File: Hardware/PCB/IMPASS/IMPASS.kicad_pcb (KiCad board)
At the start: 2 copper layers, 73.9 x 100 mm, 192 parts, among them J1 POWER, J11 SOLENOIDES, J17 PUENTE H_1, J18 PUENTE H_2, J19 SOLENOIDES, J2 POWER, J20 SENSORES, J21 PROG, J22 VM, J23 EJE1, J24 EJE2, J25 EJE3, J26 SOLENOIDES, J27 PUENTE H, J28 PUENTE H, J29 SENSORES, Q1 BC847BDW1, Q10 BC847BDW1, Q11 DMN3008SFG, Q12 DMN3008SFG, Q13 DMP3013SFV, Q14 DMP3013SFV, Q15 DMN3008SFG, Q16 DMN3008SFG, Q17 BC847BDW1, Q18 DMP3013SFV, Q19 DMN3008SFG, Q2 DMP3013SFV, Q20 DMN3008SFG, Q21 DMP3013SFV, Q22 BC847BDW1, Q23 DMN3008SFG, Q24 DMN3008SFG, Q25 DMP3013SFV, Q26 DMP3013SFV, Q3 DMP3013SFV, Q4 DMP3013SFV, Q43 DMN3008SFG, Q44 DMN3008SFG, Q45 DMN3008SFG, Q49 2N7002, Q5 BC847BDW1, Q50 2N7002, Q51 2N7002, Q52 2N7002, Q53 2N7002, Q54 2N7002, Q55 2N7002, Q56 2N7002, Q57 2N7002, Q58 2N7002, Q59 2N7002, Q6 DMP3013SFV, Q60 2N7002, Q61 2N7002, Q62 2N7002, Q63 2N7002, Q64 2N7002, Q65 2N7002, Q66 2N7002, Q67 2N7002, Q68 2N7002, Q69 2N7002, Q7 BC847BDW1, Q71 DMN3008SFG, Q73 DMN3008SFG, Q75 DMN3008SFG, Q77 DMN3008SFG, Q8 DMP3013SFV, Q9 DMP3013SFV, SW1 RESET, SW2 BOOT, U1 TPS62162DSG, U10 LIS3DH, U13 MCP3008, U14 ESP32-S3-WROOM-1, U15 TPS62163DSG, U2 LM75B, U3 ACS712xLCTR-30A, U4 ACS712xLCTR-30A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

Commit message: Hardware: Update all the logic pcb 	- added ads1015 	- added the logic foe P-MOSFET 	- added I2C connector
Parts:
- removed D1, D2, D3, D4, D5, D6: 1N4448, Diode_THT:D_DO-35_SOD27_P2.54mm_Vertical_AnodeUp
- removed D8, D9: LED, LED_SMD:LED_0603_1608Metric
- removed R21, R22, R23, R24, R25, R26: 2k, Resistor_SMD:R_0603_1608Metric
- removed R34, R85: 100, Resistor_SMD:R_0603_1608Metric
- added C29: 100nF, Capacitor_SMD:C_0603_1608Metric, F.Cu at (146.2, 101.3)
- added C30: 100nF, Capacitor_SMD:C_0603_1608Metric, F.Cu at (120.1, 123.6)
- added C31: 100nF, Capacitor_SMD:C_0603_1608Metric, F.Cu at (112.6, 123.7)
- added J30: I2C, Connector_PinHeader_2.54mm:PinHeader_1x04_P2.54mm_Horizontal, F.Cu at (122.1, 128.7)
- added R89: 10k, Resistor_SMD:R_0603_1608Metric, F.Cu at (136.2, 101.4)
- added R90: 10k, Resistor_SMD:R_0603_1608Metric, F.Cu at (137.8, 100.6)
- added R91: 36k, Resistor_SMD:R_0603_1608Metric, F.Cu at (142.2, 98.2)
- added R92: 100k, Resistor_SMD:R_0603_1608Metric, F.Cu at (138.9, 98.2)
- added R93: 47k, Resistor_SMD:R_0603_1608Metric, F.Cu at (147.8, 99.4)
- added R94: 68k, Resistor_SMD:R_0603_1608Metric, F.Cu at (145.4, 98.2)
- added R95: 10k, Resistor_SMD:R_0603_1608Metric, F.Cu at (113.9, 121.1)
- added R96: 10k, Resistor_SMD:R_0603_1608Metric, F.Cu at (118.2, 121.1)
- added R97: 10k, Resistor_SMD:R_0603_1608Metric, F.Cu at (113.7, 126.1)
- added R98: 10k, Resistor_SMD:R_0603_1608Metric, F.Cu at (117.5, 126.1)
- added R99: 10k, Resistor_SMD:R_0603_1608Metric, F.Cu at (110.9, 121.5)
- added U11: TCA9406DC, Package_SO:SSOP-8_2.95x2.8mm_P0.65mm, F.Cu at (116.3, 123.6)
- added U12: ADS1015IDGS, Package_SO:TSSOP-10_3x3mm_P0.5mm, F.Cu at (141.9, 101.2)
- moved U8 107.1 mm to (54.3, 65.0), turned to 0 degrees
- moved C23 98.0 mm to (64.5, 33.4)
- moved U7 94.7 mm to (54.3, 58.4), turned to 0 degrees
- moved C25 93.2 mm to (68.5, 25.9), turned to 0 degrees
- moved C22 88.3 mm to (64.5, 30.9)
- moved Q18 85.4 mm to (75.3, 24.6), turned to 0 degrees
- moved U6 82.5 mm to (54.3, 51.8), turned to 0 degrees
- moved Q23 81.3 mm to (86.2, 24.6), turned to 0 degrees
- moved C26 81.2 mm to (68.5, 28.4), turned to 0 degrees
- moved Q24 80.9 mm to (86.2, 29.5), turned to 0 degrees
- moved Q25 80.6 mm to (91.6, 24.6), turned to 0 degrees
- moved Q21 80.2 mm to (80.8, 29.5), turned to 0 degrees
- moved Q26 80.1 mm to (91.6, 29.5), turned to 0 degrees
- moved Q20 79.1 mm to (80.8, 24.6), turned to 0 degrees
- moved Q19 78.7 mm to (75.3, 29.5), turned to 0 degrees
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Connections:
- C4 pad 1: /12v -> +12V
- J1 pad 1: /12v -> +12V
- Q1 pad 1: GND1 -> GND
- Q1 pad 3: Net-(Q1B-C2) -> /Placa_logica/logica_puente_h/PWM1
- Q1 pad 4: GND1 -> GND
- Q1 pad 6: Net-(Q1A-C1) -> /Placa_logica/logica_puente_h/~PWM1
- Q10 pad 1: GND1 -> GND
- Q10 pad 3: Net-(Q10B-C2) -> /Placa_logica/logica_puente_h/PWM4
- Q10 pad 4: GND1 -> GND
- Q10 pad 6: Net-(Q10A-C1) -> /Placa_logica/logica_puente_h/~PWM4
- Q13 pad 4: Net-(Q10A-C1) -> /Placa_potencia/Eje2/PWM4
- Q14 pad 4: Net-(Q10B-C2) -> /Placa_potencia/Eje2/~PWM4
- Q17 pad 1: GND1 -> GND
- Q17 pad 3: Net-(Q17B-C2) -> /Placa_logica/logica_puente_h/PWM5
- Q17 pad 4: GND1 -> GND
- Q17 pad 6: Net-(Q17A-C1) -> /Placa_logica/logica_puente_h/~PWM5
- Q18 pad 4: Net-(Q17A-C1) -> /Placa_potencia/Eje3/PWM5
- Q2 pad 4: Net-(Q1A-C1) -> /Placa_potencia/Eje1/PWM1
- Q21 pad 4: Net-(Q17B-C2) -> /Placa_potencia/Eje3/~PWM5
- Q22 pad 1: GND1 -> GND
- Q22 pad 3: Net-(Q22B-C2) -> /Placa_logica/logica_puente_h/PWM6
- Q22 pad 4: GND1 -> GND
- Q22 pad 6: Net-(Q22A-C1) -> /Placa_logica/logica_puente_h/~PWM6
- Q25 pad 4: Net-(Q22A-C1) -> /Placa_potencia/Eje3/PWM6
- Q26 pad 4: Net-(Q22B-C2) -> /Placa_potencia/Eje3/~PWM6
- Q3 pad 4: Net-(Q1B-C2) -> /Placa_potencia/Eje1/~PWM1
- Q4 pad 4: Net-(Q4-G) -> /Placa_potencia/Eje1/PWM2
- Q5 pad 1: GND1 -> GND
- Q5 pad 3: Net-(Q5B-C2) -> /Placa_logica/logica_puente_h/PWM2
- Q5 pad 4: GND1 -> GND
- Q5 pad 6: Net-(Q4-G) -> /Placa_logica/logica_puente_h/~PWM2
- Q50 pad 3: /Placa_logica/logica_puente_h/~PWM1 -> Net-(Q50-D)
- Q51 pad 3: /Placa_logica/logica_puente_h/PWM1 -> Net-(Q51-D)
- Q53 pad 3: /Placa_logica/logica_puente_h/~PWM2 -> Net-(Q53-D)
- Q54 pad 3: /Placa_logica/logica_puente_h/PWM2 -> Net-(Q54-D)
- Q56 pad 3: /Placa_logica/logica_puente_h/~PWM3 -> Net-(Q56-D)
- Q57 pad 3: /Placa_logica/logica_puente_h/PWM3 -> Net-(Q57-D)
- Q6 pad 4: Net-(Q5B-C2) -> /Placa_potencia/Eje1/~PWM2
- Q61 pad 3: /Placa_logica/logica_puente_h/~PWM4 -> Net-(Q61-D)
- Q62 pad 3: /Placa_logica/logica_puente_h/~PWM5 -> Net-(Q62-D)
- Q63 pad 3: /Placa_logica/logica_puente_h/~PWM6 -> Net-(Q63-D)
- Q64 pad 3: /Placa_logica/logica_puente_h/PWM4 -> Net-(Q64-D)
- Q65 pad 3: /Placa_logica/logica_puente_h/PWM5 -> Net-(Q65-D)
- Q66 pad 3: /Placa_logica/logica_puente_h/PWM6 -> Net-(Q66-D)
- Q7 pad 1: GND1 -> GND
- Q7 pad 3: Net-(Q7B-C2) -> /Placa_logica/logica_puente_h/PWM3
- Q7 pad 4: GND1 -> GND
- Q7 pad 6: Net-(Q7A-C1) -> /Placa_logica/logica_puente_h/~PWM3
- Q8 pad 4: Net-(Q7A-C1) -> /Placa_potencia/Eje2/PWM3
- Q9 pad 4: Net-(Q7B-C2) -> /Placa_potencia/Eje2/~PWM3
- R36 pad 2: /Placa_logica/logica_puente_h/~PWM1 -> Net-(Q50-D)
- R37 pad 2: /Placa_logica/logica_puente_h/PWM1 -> Net-(Q51-D)
- R39 pad 2: /Placa_logica/logica_puente_h/~PWM2 -> Net-(Q53-D)
- R40 pad 2: /Placa_logica/logica_puente_h/PWM2 -> Net-(Q54-D)
- R42 pad 2: /Placa_logica/logica_puente_h/~PWM3 -> Net-(Q56-D)
- R43 pad 2: /Placa_logica/logica_puente_h/PWM3 -> Net-(Q57-D)
- R47 pad 2: /Placa_logica/logica_puente_h/~PWM4 -> Net-(Q61-D)
- R48 pad 2: /Placa_logica/logica_puente_h/~PWM5 -> Net-(Q62-D)
- R49 pad 2: /Placa_logica/logica_puente_h/~PWM6 -> Net-(Q63-D)
- R50 pad 2: /Placa_logica/logica_puente_h/PWM4 -> Net-(Q64-D)
- R51 pad 2: /Placa_logica/logica_puente_h/PWM5 -> Net-(Q65-D)
- R52 pad 2: /Placa_logica/logica_puente_h/PWM6 -> Net-(Q66-D)
- R59 pad 1: 12v -> /Placa_logica/logica_puente_h/~PWM1
- R59 pad 2: Net-(Q1A-C1) -> +12V
- R60 pad 1: 12v -> /Placa_logica/logica_puente_h/PWM1
- R60 pad 2: Net-(Q1B-C2) -> +12V
- R61 pad 1: /Placa_potencia/Eje1/PWM1 -> Net-(Q50-D)
- R62 pad 2: /Placa_potencia/Eje1/~PWM1 -> Net-(Q51-D)
- R63 pad 1: /Placa_potencia/Eje1/PWM2 -> Net-(Q53-D)
- R64 pad 1: 12v -> /Placa_logica/logica_puente_h/~PWM2
- R64 pad 2: Net-(Q4-G) -> +12V
- R65 pad 1: 12v -> /Placa_logica/logica_puente_h/PWM2
- R65 pad 2: Net-(Q5B-C2) -> +12V
- R66 pad 2: /Placa_potencia/Eje1/~PWM2 -> Net-(Q54-D)
- R67 pad 1: /Placa_potencia/Eje2/PWM3 -> Net-(Q56-D)
- R68 pad 1: 12v -> /Placa_logica/logica_puente_h/~PWM3
- R68 pad 2: Net-(Q7A-C1) -> +12V
- R69 pad 1: 12v -> /Placa_logica/logica_puente_h/PWM3
- R69 pad 2: Net-(Q7B-C2) -> +12V
- R70 pad 2: /Placa_potencia/Eje2/~PWM3 -> Net-(Q57-D)
- R71 pad 1: /Placa_potencia/Eje2/PWM4 -> Net-(Q61-D)
- R72 pad 1: 12v -> /Placa_logica/logica_puente_h/~PWM4
- R72 pad 2: Net-(Q10A-C1) -> +12V
- R73 pad 1: 12v -> /Placa_logica/logica_puente_h/PWM4
- R73 pad 2: Net-(Q10B-C2) -> +12V
- R74 pad 2: /Placa_potencia/Eje2/~PWM4 -> Net-(Q64-D)
- R75 pad 1: /Placa_potencia/Eje3/PWM5 -> Net-(Q62-D)
- R76 pad 1: 12v -> /Placa_logica/logica_puente_h/~PWM5
- R76 pad 2: Net-(Q17A-C1) -> +12V
- R77 pad 1: 12v -> /Placa_logica/logica_puente_h/PWM5
- R77 pad 2: Net-(Q17B-C2) -> +12V
- R78 pad 2: /Placa_potencia/Eje3/~PWM5 -> Net-(Q65-D)
- R79 pad 1: /Placa_potencia/Eje3/PWM6 -> Net-(Q63-D)
- R80 pad 1: 12v -> /Placa_logica/logica_puente_h/~PWM6
- R80 pad 2: Net-(Q22A-C1) -> +12V
- R81 pad 1: 12v -> /Placa_logica/logica_puente_h/PWM6
- R81 pad 2: Net-(Q22B-C2) -> +12V
- R82 pad 2: /Placa_potencia/Eje3/~PWM6 -> Net-(Q66-D)
- U15 pad 2: /12v -> +12V
- U15 pad 3: /12v -> +12V
- U3 pad 7: Net-(U3-VIOUT) -> /Placa_potencia/Sensores_potencia/I_1
- U4 pad 7: Net-(U4-VIOUT) -> /Placa_potencia/Sensores_potencia/I_2
- U5 pad 7: Net-(U5-VIOUT) -> /Placa_potencia/Sensores_potencia/I_3
- U6 pad 7: Net-(U6-VIOUT) -> /Placa_potencia/Sensores_potencia/I_4
- U7 pad 7: Net-(U7-VIOUT) -> /Placa_potencia/Sensores_potencia/I_5
- U8 pad 7: Net-(U8-VIOUT) -> /Placa_potencia/Sensores_potencia/I_6
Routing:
- net GND1: track 420.8 -> 110.2 mm, vias 18 -> 1
- net +12V: track 0.00 -> 202.8 mm, vias 0 -> 28
- net 12v: track 244.9 -> 63.3 mm, vias 4 -> 0
- net /Placa_potencia/Sensores_potencia/SCL: track 118.1 -> 2.57 mm, vias 1 -> 0
- net /Placa_potencia/Sensores_potencia/5V: track 117.9 -> 7.83 mm, vias 10 -> 0
- net GND: track 399.8 -> 486.7 mm, vias 13 -> 18
- net /Placa_potencia/Sensores_potencia/SDA: track 89.1 -> 3.85 mm, vias 1 -> 0
- net +3.3V: track 208.2 -> 271.0 mm, vias 5 -> 18
- net /Placa_potencia/Sensores_potencia/3.3V: track 57.8 -> 0.00 mm, vias 1 -> 0
- net /Placa_potencia/Sensores_potencia/OUT6_2: track 57.6 -> 0.00 mm, vias 1 -> 0
- net /Placa_potencia/Eje3/OUT6_2: track 51.0 -> 0.00 mm, vias 2 -> 0
- net /Placa_potencia/Sensores_potencia/I_4: track 40.8 -> 0.92 mm
- net /Placa_potencia/Sensores_potencia/OUT5_2: track 37.7 -> 0.00 mm, vias 2 -> 0
- net /Placa_potencia/Sensores_potencia/I_3: track 34.9 -> 0.00 mm, vias 4 -> 0
- net /Placa_potencia/Eje2/OUT4_2: track 34.7 -> 0.00 mm, vias 2 -> 0
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- removed copper zone on B.Cu, net GND1
- removed copper zone on F.Cu, net GND1

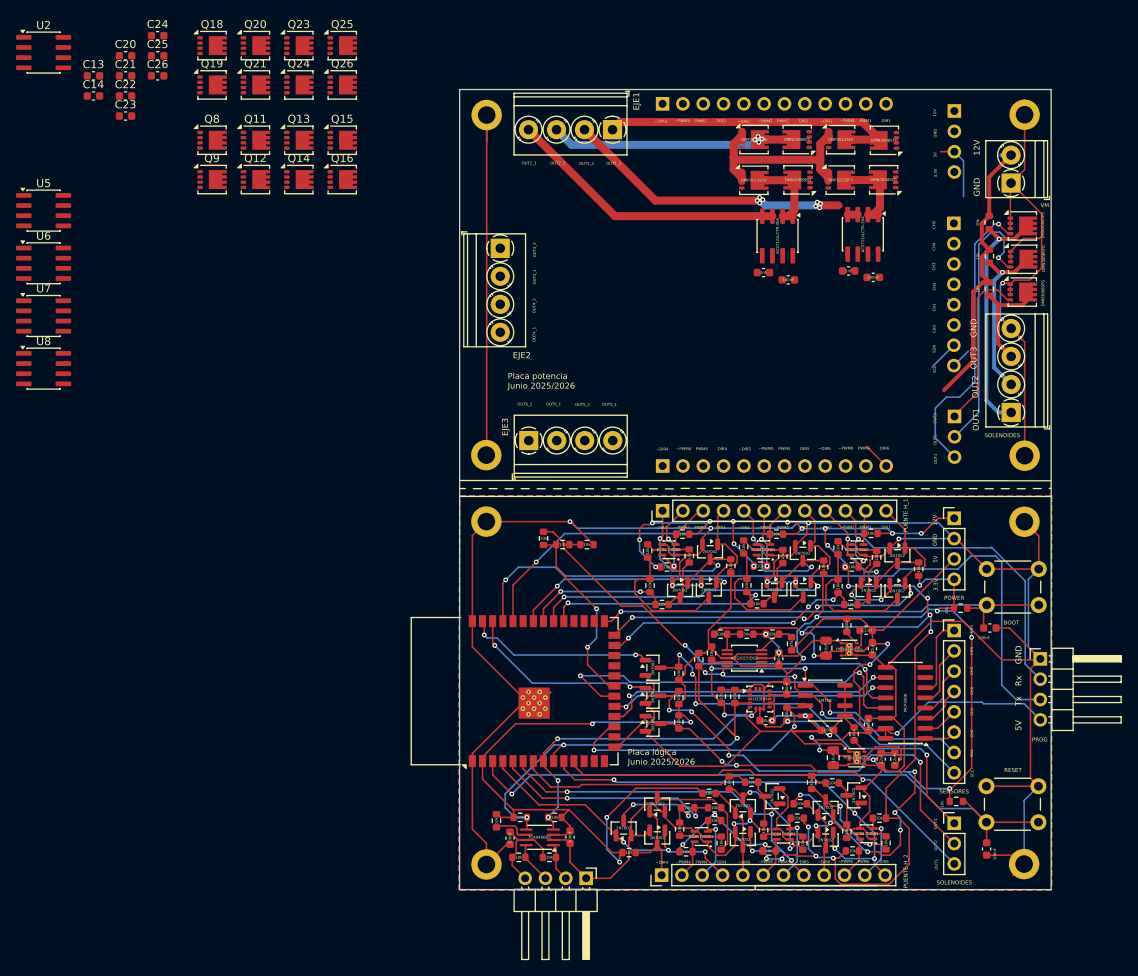
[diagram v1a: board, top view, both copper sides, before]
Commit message: Hardware: Update all the power pcb 	- added thr MOSFETs         - added the current sensors         - added the lm75 sensor
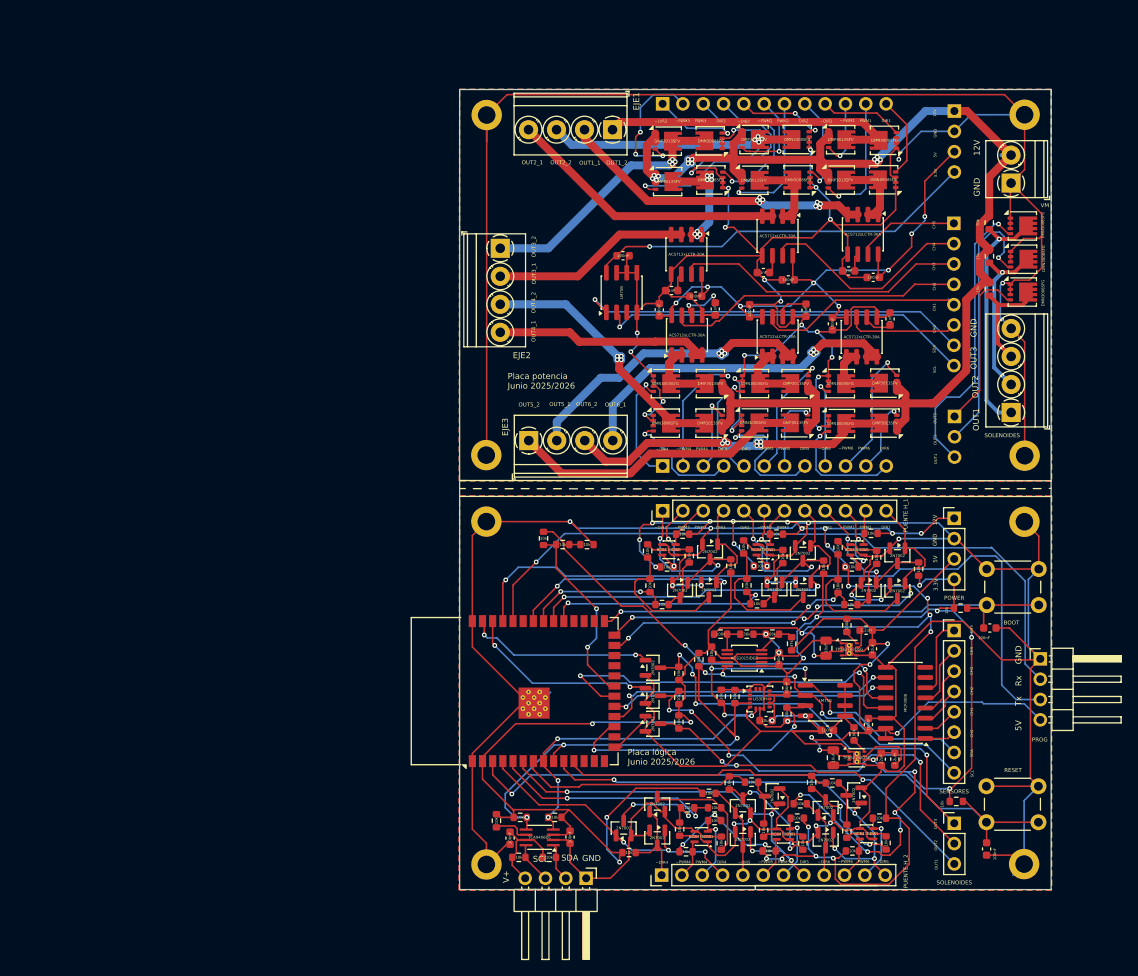
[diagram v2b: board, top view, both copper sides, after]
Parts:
- moved U8 102.3 mm to (156.6, 61.0), turned to 90 degrees
- moved C25 97.3 mm to (160.1, 58.8), turned to 90 degrees
- moved C23 92.1 mm to (152.9, 59.4), turned to -90 degrees
- moved U7 91.8 mm to (146.1, 61.0), turned to 90 degrees
- moved C26 86.2 mm to (149.6, 57.7), turned to -90 degrees
- moved Q18 84.3 mm to (148.3, 66.9), turned to 180 degrees
- moved C22 82.5 mm to (142.6, 57.8), turned to 90 degrees
- moved U6 80.9 mm to (134.7, 60.8), turned to 90 degrees
- moved U5 80.5 mm to (134.6, 50.7), turned to -90 degrees
- moved C13 80.2 mm to (135.8, 56.0), turned to 180 degrees
- moved Q26 79.9 mm to (159.5, 71.8), turned to 180 degrees
- moved Q25 79.9 mm to (159.4, 66.8), turned to 180 degrees
- moved Q24 79.8 mm to (153.9, 71.9)
- moved Q23 79.8 mm to (153.9, 66.9)
- moved Q21 79.6 mm to (148.3, 71.8), turned to 180 degrees
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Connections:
- net Net-(J30-Pin_2) renamed /Placa_logica/SDA_b
- net Net-(J30-Pin_3) renamed /Placa_logica/SCL_b
- J25 pad 1: /Placa_potencia/Eje3/OUT6_2 -> /Placa_potencia/Eje3/OUT5_2
- J25 pad 2: /Placa_potencia/Sensores_potencia/OUT6_2 -> /Placa_potencia/Sensores_potencia/OUT5_2
- J25 pad 3: /Placa_potencia/Eje3/OUT5_2 -> /Placa_potencia/Eje3/OUT6_2
- J25 pad 4: /Placa_potencia/Sensores_potencia/OUT5_2 -> /Placa_potencia/Sensores_potencia/OUT6_2
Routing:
- net GND1: track 110.2 -> 428.3 mm, vias 1 -> 23
- net 12v: track 63.3 -> 165.0 mm, vias 0 -> 12
- net /Placa_potencia/Sensores_potencia/5V: track 7.83 -> 77.5 mm, vias 0 -> 8
- net /Placa_potencia/Sensores_potencia/3.3V: track 0.00 -> 49.3 mm, vias 0 -> 1
- net /Placa_potencia/Sensores_potencia/SDA: track 3.85 -> 49.6 mm, vias 0 -> 1
- net /Placa_potencia/Eje3/OUT6_2: track 0.00 -> 44.7 mm, vias 0 -> 7
- net /Placa_potencia/Sensores_potencia/SCL: track 2.57 -> 47.0 mm, vias 0 -> 1
- net /Placa_potencia/Sensores_potencia/OUT6_2: track 0.00 -> 44.0 mm, vias 0 -> 4
- net /Placa_potencia/Sensores_potencia/OUT5_2: track 0.00 -> 38.9 mm, vias 0 -> 4
- net /Placa_potencia/Sensores_potencia/I_4: track 0.92 -> 38.2 mm
- net /Placa_potencia/Eje3/OUT5_2: track 0.72 -> 37.5 mm
- net /Placa_potencia/Sensores_potencia/I_3: track 0.00 -> 36.8 mm
- net /Placa_potencia/Eje2/OUT4_2: track 0.00 -> 34.4 mm, vias 0 -> 4
- net /Placa_potencia/Eje2/OUT3_2: track 0.00 -> 33.5 mm, vias 0 -> 4
- net /Placa_potencia/Eje2/PWM3: track 0.00 -> 30.8 mm, vias 0 -> 1
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- added copper zone on B.Cu, net GND1
- added copper zone on F.Cu, net GND1
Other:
- board text added: "V+"
